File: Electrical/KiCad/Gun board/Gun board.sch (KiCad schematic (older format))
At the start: 73 parts

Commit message: added resistor values for SPI Switch
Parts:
- J?: symbol Connector:Micro_SD_Card -> Gun-board-rescue:Micro_SD_Card-Connector
- R? (x2): value R -> 10kΩ
- R? (x2): value R -> 4.7kΩ
- U? (x2): symbol Gun-board-rescue:AAT1217-aat1217.lib-Gun-board-rescue -> Gun-board-rescue:AAT1217-aat1217.lib-Gun-board-rescue-Gun-board-rescue
- U?: symbol Gun-board-rescue:STM32F030F4Px-MCU_ST_STM32F0 -> Gun-board-rescue:STM32F030F4Px-MCU_ST_STM32F0-Gun-board-rescue
- U?: symbol custom_components:MCP4725 -> Gun-board-rescue:MCP4725-custom_components
- U?: symbol custom_components:MCP4018 -> Gun-board-rescue:MCP4018-custom_components
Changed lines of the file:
@@
 EESchema Schematic File Version 4
 LIBS:Gun board-cache
-EELAYER 29 0
+EELAYER 26 0
 EELAYER END
 $Descr USLetter 11000 8500
@@
 $EndComp
 $Comp
-L Gun-board-rescue:AAT1217-aat1217.lib-Gun-board-rescue U?
+L Gun-board-rescue:AAT1217-aat1217.lib-Gun-board-rescue-Gun-board-rescue U?
 U 1 1 5CB9C019
 P 1700 1300
@@
 $EndComp
 $Comp
-L Gun-board-rescue:AAT1217-aat1217.lib-Gun-board-rescue U?
+L Gun-board-rescue:AAT1217-aat1217.lib-Gun-board-rescue-Gun-board-rescue U?
 U 1 1 5CB12524
 P 1500 3150
@@
 $EndComp
 $Comp
-L Gun-board-rescue:+3V-custom_power-Gun-board-rescue #PWR?
+L Gun-board-rescue:+3V-custom_power-Gun-board-rescue-Gun-board-rescue #PWR?
 U 1 1 5CC0972E
 P 1850 6600
@@
 $EndComp
 $Comp
-L Gun-board-rescue:GND-custom_power-Gun-board-rescue #PWR?
+L Gun-board-rescue:GND-custom_power-Gun-board-rescue-Gun-board-rescue #PWR?
 U 1 1 5CC09FE8
 P 1850 7750
@@
 	6850 1750 6950 1750
 $Comp
-L Gun-board-rescue:STM32F030F4Px-MCU_ST_STM32F0 U?
+L Gun-board-rescue:STM32F030F4Px-MCU_ST_STM32F0-Gun-board-rescue U?
 U 1 1 5CB198C5
 P 5250 1650
@@
 $EndComp
 $Comp
-L Gun-board-rescue:GND-custom_power-Gun-board-rescue #PWR?
+L Gun-board-rescue:GND-custom_power-Gun-board-rescue-Gun-board-rescue #PWR?
 U 1 1 5CC02426
 P 2550 5600
@@
 	2100 5300 2550 5300
 $Comp
-L Gun-board-rescue:GND-custom_power-Gun-board-rescue #PWR?
+L Gun-board-rescue:GND-custom_power-Gun-board-rescue-Gun-board-rescue #PWR?
 U 1 1 5CBFEF57
 P 2100 5900
@@
 $EndComp
 $Comp
-L Gun-board-rescue:+3V-custom_power-Gun-board-rescue #PWR?
+L Gun-board-rescue:+3V-custom_power-Gun-board-rescue-Gun-board-rescue #PWR?
 U 1 1 5CBFAAE2
 P 2550 5300
@@
 $EndComp
 $Comp
-L custom_power:GND #PWR?
+L Gun-board-rescue:GND-custom_power #PWR?
 U 1 1 5CBED840
 P 9950 3550
@@
 $EndComp
 $Comp
-L custom_power:+3.3V #PWR?
+L Gun-board-rescue:+3.3V-custom_power #PWR?
 U 1 1 5CBED83A
 P 9950 2850
@@
 $EndComp
 $Comp
-L custom_power:GND #PWR?
+L Gun-board-rescue:GND-custom_power #PWR?
 U 1 1 5CBA2547
 P 9950 2350
@@
 $EndComp
 $Comp
-L custom_power:+3.3V #PWR?
+L Gun-board-rescue:+3.3V-custom_power #PWR?
 U 1 1 5CBA1B30
 P 9950 1850
@@
 $EndComp
 $Comp
-L custom_power:+3.3V #PWR?
+L Gun-board-rescue:+3.3V-custom_power #PWR?
 U 1 1 5CDF6904
 P 9950 4100
@@
 $EndComp
 $Comp
-L custom_power:GND #PWR?
+L Gun-board-rescue:GND-custom_power #PWR?
 U 1 1 5CDF737B
 P 9950 4400
@@
 	9750 4250 9800 4250
 $Comp
-L Connector:Micro_SD_Card J?
+L Gun-board-rescue:Micro_SD_Card-Connector J?
 U 1 1 5CD7984C
 P 9600 5900
@@
 CE1
 $Comp
-L custom_power:+3.3V #PWR?
+L Gun-board-rescue:+3.3V-custom_power #PWR?
 U 1 1 5CDA1BCA
 P 8550 5900
@@
 SCK
 $Comp
-L custom_power:GND #PWR?
+L Gun-board-rescue:GND-custom_power #PWR?
 U 1 1 5CDA338C
 P 8550 6100
@@
 	8550 6200 8700 6200
 $Comp
-L custom_power:GND #PWR?
+L Gun-board-rescue:GND-custom_power #PWR?
 U 1 1 5CDC79B8
 P 10400 6500
@@
 	4100 3750 4200 3750
 $Comp
-L custom_power:GND #PWR?
+L Gun-board-rescue:GND-custom_power #PWR?
 U 1 1 5CDE7E11
 P 4100 3750
@@
 $EndComp
 $Comp
-L custom_power:+3.3V #PWR?
+L Gun-board-rescue:+3.3V-custom_power #PWR?
 U 1 1 5CDE6399
 P 4100 3550
@@
 	7650 5400 8050 5400
 $Comp
-L custom_power:+3.3V #PWR?
+L Gun-board-rescue:+3.3V-custom_power #PWR?
 U 1 1 5CC34465
 P 6350 6100
@@
 P 6700 6100
 F 0 "R?" V 6493 6100 50  0000 C CNN
-F 1 "R" V 6584 6100 50  0000 C CNN
+F 1 "10kΩ" V 6584 6100 50  0000 C CNN
 F 2 "" V 6630 6100 50  0001 C CNN
 F 3 "~" H 6700 6100 50  0001 C CNN
@@
 P 7500 5900
 F 0 "R?" V 7293 5900 50  0000 C CNN
-F 1 "R" V 7384 5900 50  0000 C CNN
+F 1 "4.7kΩ" V 7384 5900 50  0000 C CNN
 F 2 "" V 7430 5900 50  0001 C CNN
 F 3 "~" H 7500 5900 50  0001 C CNN
@@
 $EndComp
 $Comp
-L custom_power:GND #PWR?
+L Gun-board-rescue:GND-custom_power #PWR?
 U 1 1 5CC4FC70
 P 7050 5700
@@
 	6350 5200 5950 5200
 $Comp
-L custom_power:GND #PWR?
+L Gun-board-rescue:GND-custom_power #PWR?
 U 1 1 5CC31331
 P 6350 4900
@@
 P 6800 5400
 F 0 "R?" V 6593 5400 50  0000 C CNN
-F 1 "R" V 6684 5400 50  0000 C CNN
+F 1 "4.7kΩ" V 6684 5400 50  0000 C CNN
 F 2 "" V 6730 5400 50  0001 C CNN
 F 3 "~" H 6800 5400 50  0001 C CNN
@@
 P 6350 5050
 F 0 "R?" V 6143 5050 50  0000 C CNN
-F 1 "R" V 6234 5050 50  0000 C CNN
+F 1 "10kΩ" V 6234 5050 50  0000 C CNN
 F 2 "" V 6280 5050 50  0001 C CNN
 F 3 "~" H 6350 5050 50  0001 C CNN
@@
 I2C_SDA
 $Comp
-L custom_power:GND #PWR?
+L Gun-board-rescue:GND-custom_power #PWR?
 U 1 1 5CFA5BBD
 P 6400 3650
@@
 $EndComp
 $Comp
-L custom_power:+3.3V #PWR?
+L Gun-board-rescue:+3.3V-custom_power #PWR?
 U 1 1 5CFA5996
 P 6400 3450
@@
 	8000 3650 8200 3650
 $Comp
-L custom_power:GND #PWR?
+L Gun-board-rescue:GND-custom_power #PWR?
 U 1 1 5CF8B068
 P 8200 4350
@@
 	8700 3750 8700 3900
 $Comp
-L custom_power:GND #PWR?
+L Gun-board-rescue:GND-custom_power #PWR?
 U 1 1 5CF7D7A0
 P 8700 3900
@@
 	7150 3250 7150 3450
 $Comp
-L custom_power:GND #PWR?
+L Gun-board-rescue:GND-custom_power #PWR?
 U 1 1 5CF53E7D
 P 7600 3950
@@
 $EndComp
 $Comp
-L custom_power:GND #PWR?
+L Gun-board-rescue:GND-custom_power #PWR?
 U 1 1 5CF531DF
 P 7400 3750
@@
 SPK
 $Comp
-L custom_power:+5V #PWR?
+L Gun-board-rescue:+5V-custom_power #PWR?
 U 1 1 5CF50F83
 P 7600 3350
@@
 $EndComp
 $Comp
-L custom_components:MCP4018 U?
+L Gun-board-rescue:MCP4018-custom_components U?
 U 1 1 5CF2C1FE
 P 6800 3550
@@
 Connection ~ 7650 5400
 $Comp
-L custom_power:+3.3V #PWR?
+L Gun-board-rescue:+3.3V-custom_power #PWR?
 U 1 1 5CE8FC7C
 P 5500 3350
@@
 Connection ~ 4200 3550
 $Comp
-L custom_components:MCP4725 U?
+L Gun-board-rescue:MCP4725-custom_components U?
 U 1 1 5CE30293
 P 4550 3650

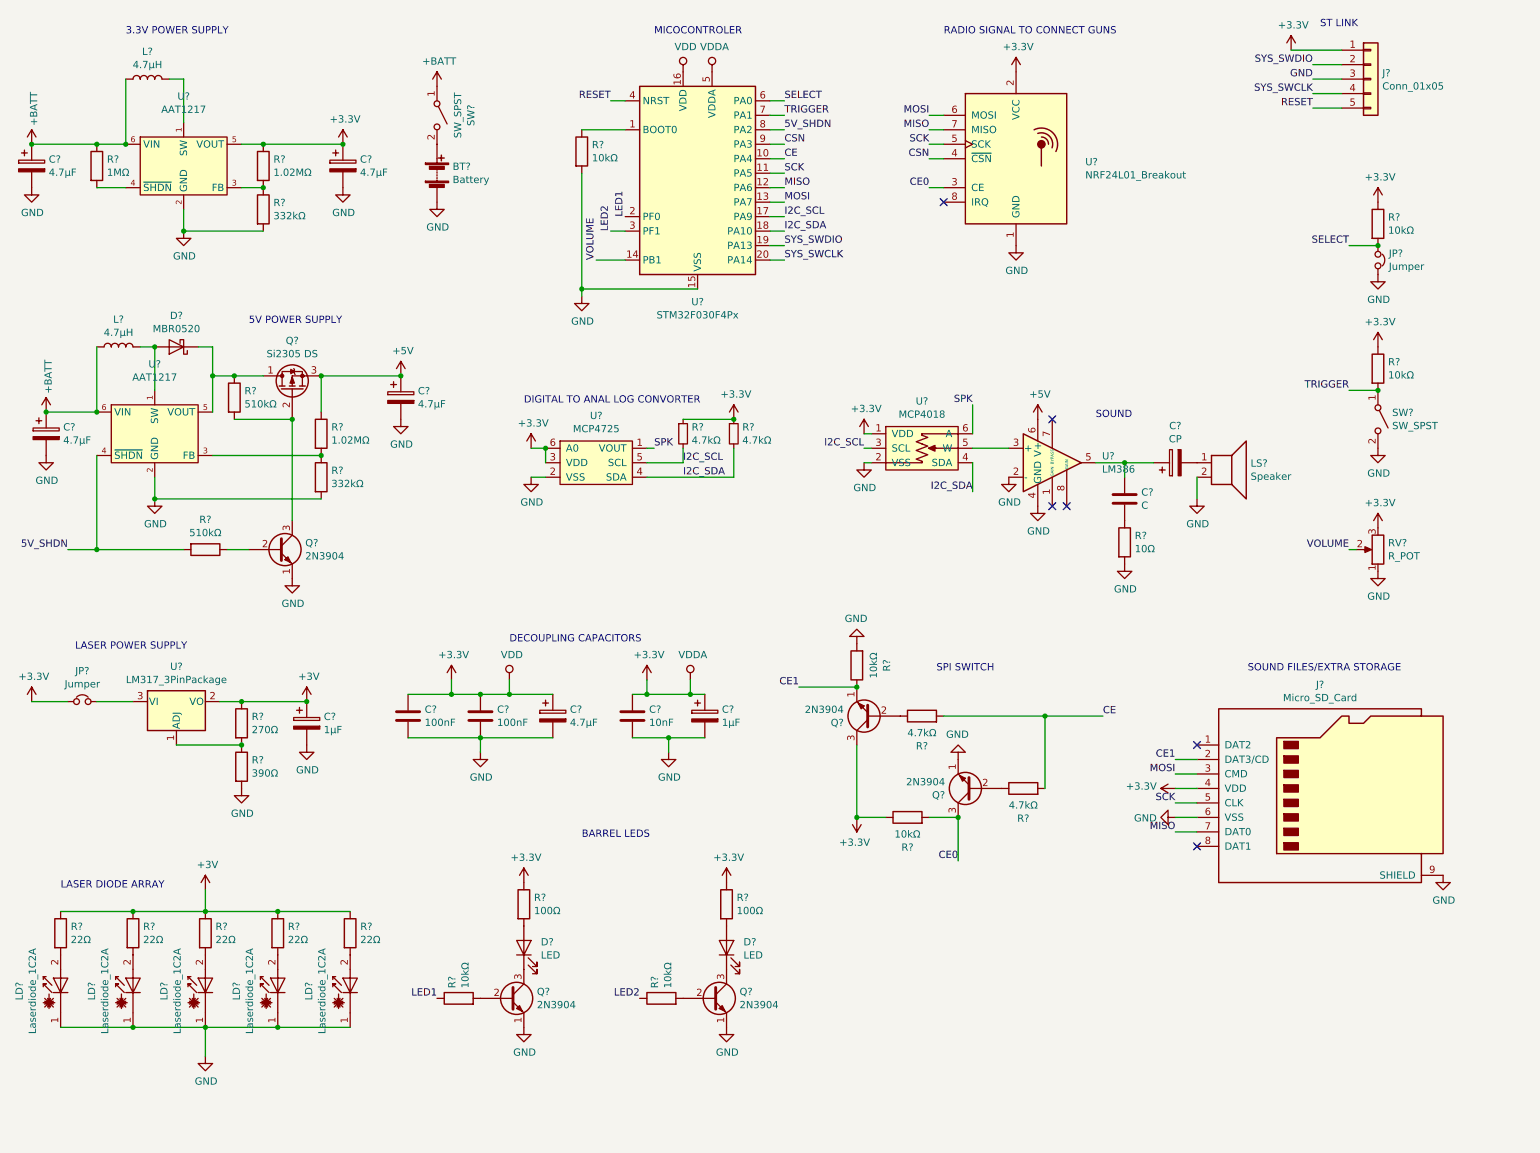
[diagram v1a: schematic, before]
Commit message: minor tweaks to aid finding parts for prototype
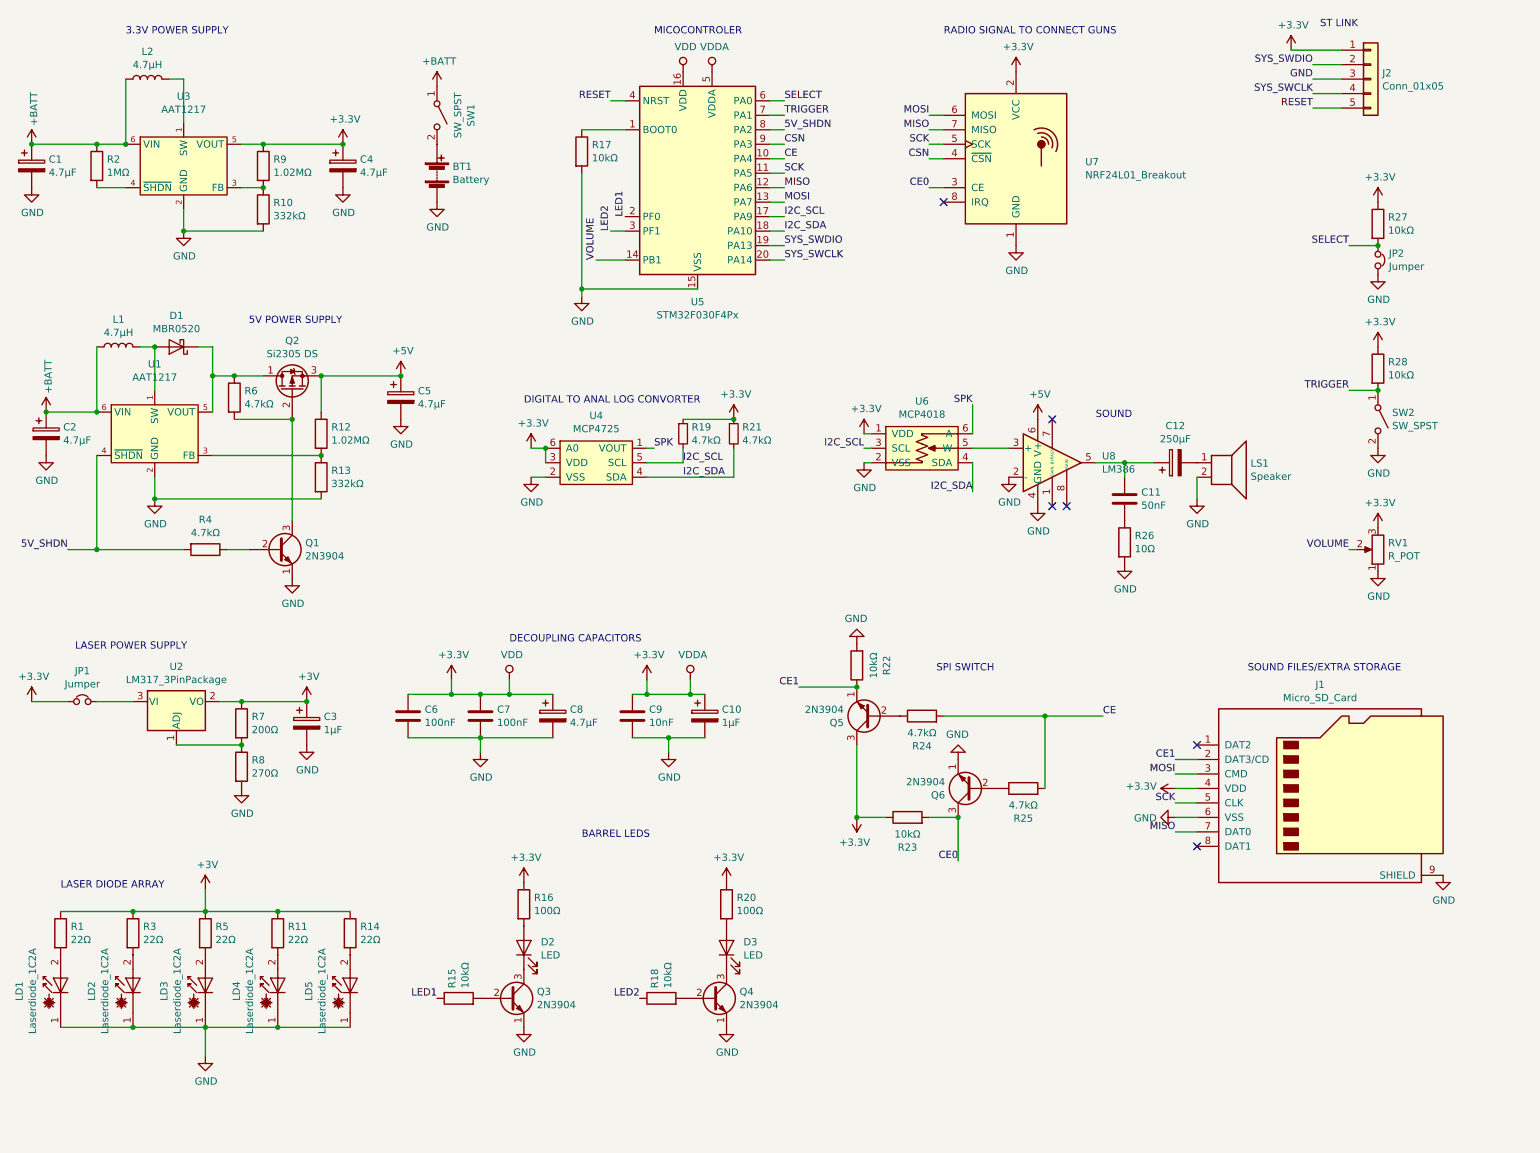
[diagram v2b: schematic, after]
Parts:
- C11: renamed from C?; value C -> 50nF
- C12: renamed from C?; value CP -> 250μF
- R4, R6: renamed from R?; value 510kΩ -> 4.7kΩ
- R7: renamed from R?; value 270Ω -> 200Ω
- R8: renamed from R?; value 390Ω -> 270Ω
- gave numbers to parts that had none: 67

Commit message: Simplified Schematic
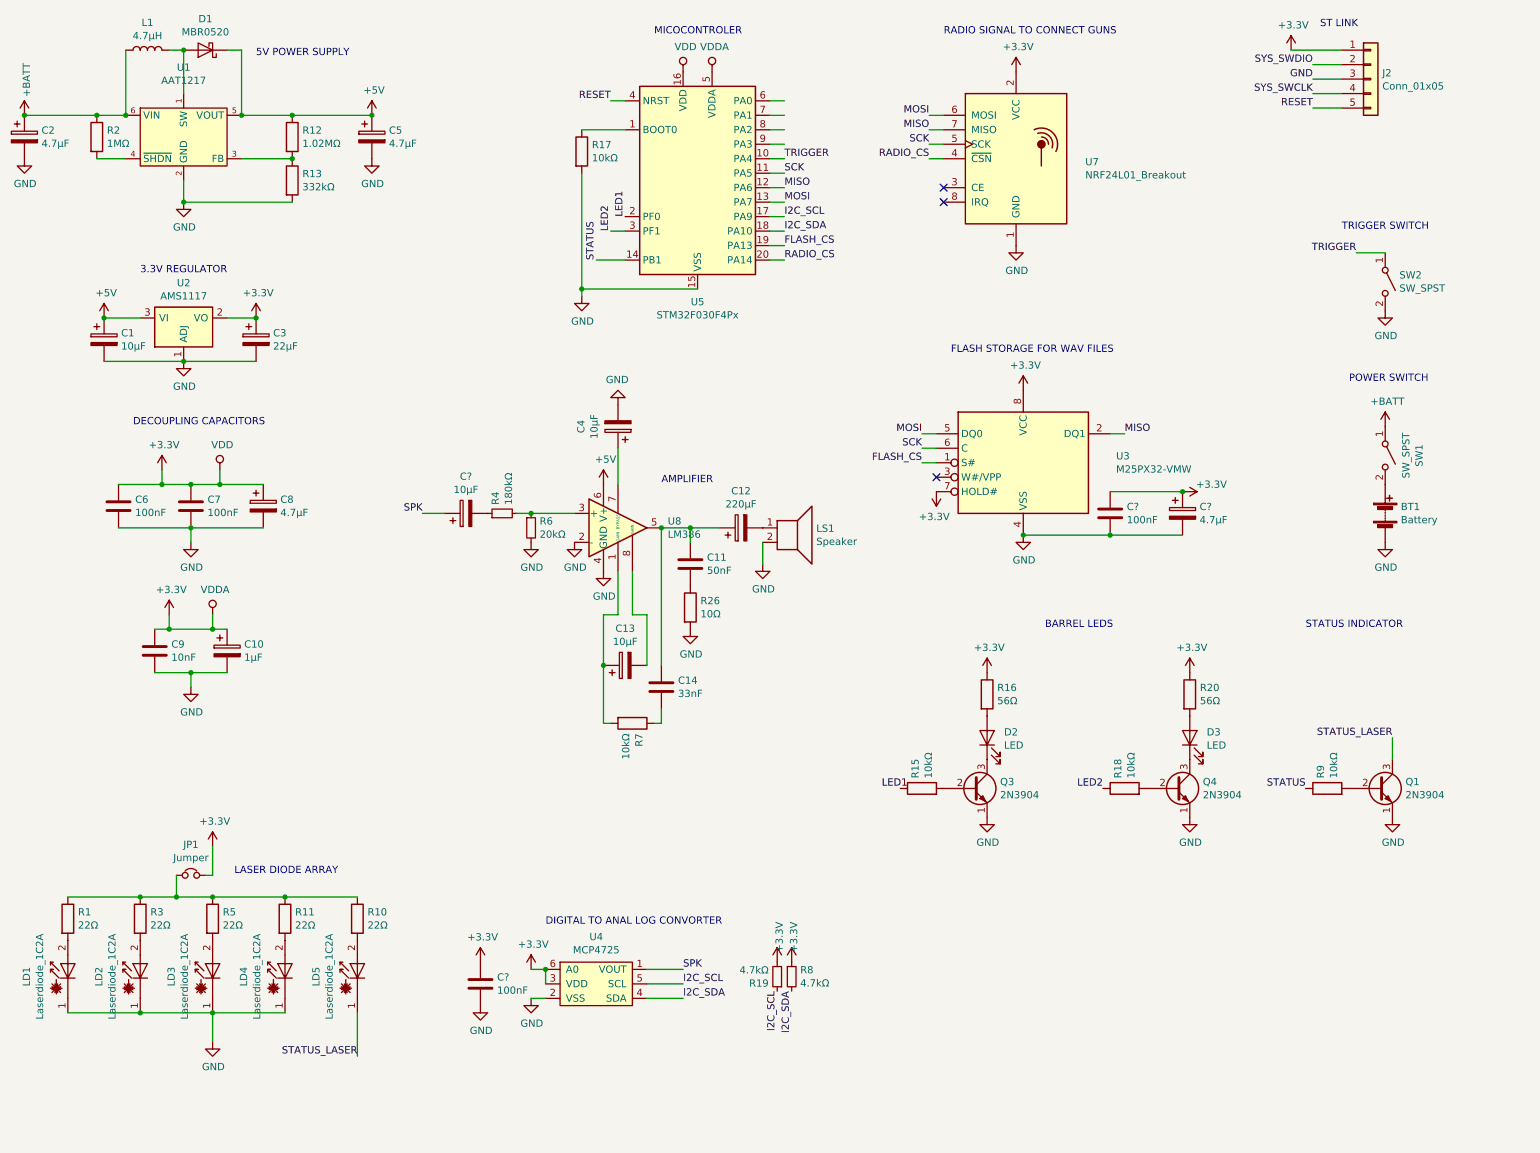
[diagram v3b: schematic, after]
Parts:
- removed J1: Micro_SD_Card, symbol Gun-board-rescue:Micro_SD_Card-Connector
- removed JP2: Jumper, symbol Device:Jumper_NC_Small
- removed L2: 4.7μH, symbol Device:L
- removed Q2: Si2305 DS, symbol Device:Q_PMOS_DGS
- removed Q5, Q6: 2N3904, Package_TO_SOT_THT:TO-92_Inline, symbol Transistor_BJT:2N3904
- removed R14: 22Ω, symbol Device:R
- removed R21: 4.7kΩ, symbol Device:R_Small
- removed R22, R23, R27, R28: 10kΩ, symbol Device:R
- removed R24, R25, R4, R6: 4.7kΩ, symbol Device:R
- removed R8: 270Ω, symbol Device:R
- removed RV1: R_POT, symbol Device:R_POT
- removed U2: LM317_3PinPackage, symbol Regulator_Linear:LM317_3PinPackage
- removed U3: AAT1217, SOT23-6, symbol Gun-board-rescue:AAT1217-aat1217.lib-Gun-board-rescue-Gun-board-rescue
- removed U6: MCP4018, symbol Gun-board-rescue:MCP4018-custom_components
- added C13, C?: 10μF, symbol Device:CP
- added C14: 33nF, symbol Device:C
- added C? (x2): 100nF, symbol Device:C
- added C?: 4.7μF, symbol Device:CP
- added R4: 180kΩ, symbol Device:R_Small
- added R6: 20kΩ, symbol Device:R_Small
- added R8: 4.7kΩ, symbol Device:R_Small
- added U2: AMS1117, Package_TO_SOT_SMD:SOT-223-3_TabPin2, symbol Regulator_Linear:AMS1117
- added U3: M25PX32-VMW, Package_SO:SOIJ-8_5.3x5.3mm_P1.27mm, symbol Memory_Flash:M25PX32-VMW
- C1, C4: value 4.7μF -> 10μF
- C12: value 250μF -> 220μF
- C3: value 1μF -> 22μF
- R10: value 332kΩ -> 22Ω
- R16, R20: value 100Ω -> 56Ω
- R7: value 200Ω -> 10kΩ
- R9: value 1.02MΩ -> 10kΩ
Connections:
- net labels added: FLASH_CS, RADIO_CS, STATUS, STATUS_LASER
- net labels removed: +3V, 5V_SHDN, CE, CE0, CE1, CSN, SELECT, VOLUME
- wire segments 128 -> 109
- no-connect marks 6 -> 3
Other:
- note added: "3.3V REGULATOR"
- note added: "AMPLIFIER"
- note added: "FLASH STORAGE FOR WAV FILES"
- note added: "POWER SWITCH"
- note added: "STATUS INDICATOR"
- note added: "TRIGGER SWITCH"
- note removed: "3.3V POWER SUPPLY"
- note removed: "LASER POWER SUPPLY"
- note removed: "SOUND"
- note removed: "SOUND FILES/EXTRA STORAGE"
- note removed: "SPI SWITCH"
- moved on the sheet: BT1, C10, C11, C12, C2, C5, C6, C7, C8, C9, D1, D2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
